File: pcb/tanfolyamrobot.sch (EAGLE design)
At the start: 86 parts, among them IC1 STM32F10XRXT6, IC2 7805, IC4 FT232RL, IC5 LD117AS33TR, M1 DRV8833, Q1 AO4407A, Q2 BSS123, Q3 BSS123, Q4 BSS123, X1 CSTCE08M, X2 PWR, X6 KUSBVX-BS1N

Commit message: fixed silkscreen
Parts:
- renumbered JP1 to SWD, JP16 to SERVO, LED1 to TX, LED2 to RX, S1 to RST, S2 to BUT, VR1 to CONT

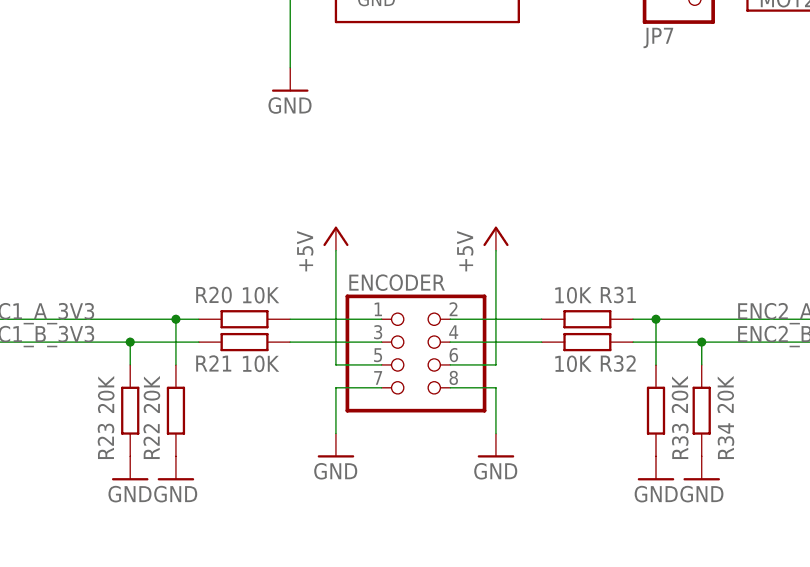
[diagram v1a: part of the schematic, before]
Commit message: fixed encoder connector silkscreen
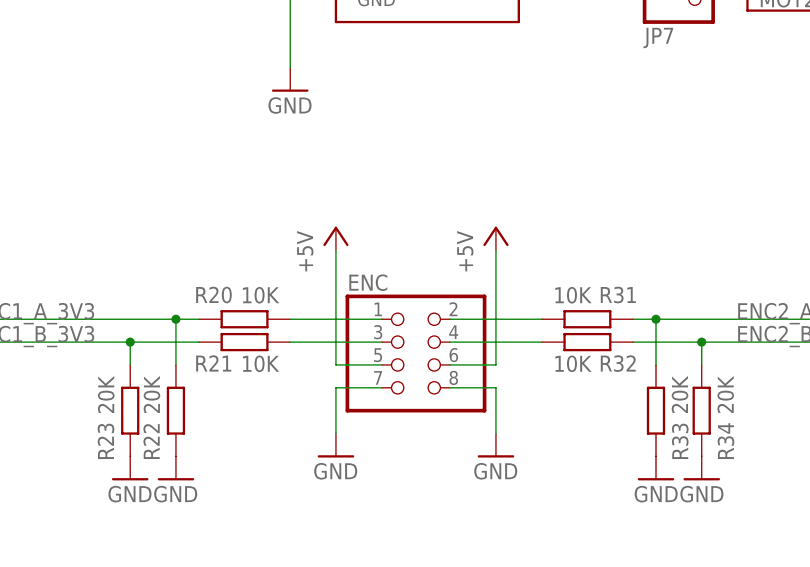
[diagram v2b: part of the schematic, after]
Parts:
- renumbered ENCODER to ENC
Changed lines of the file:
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@@
 <part name="IC5" library="v-reg" library_urn="urn:adsk.eagle:library:409" deviceset="LD117A?*" device="S" package3d_urn="urn:adsk.eagle:package:30370/1" technology="33TR"/>
 <part name="SERVO" library="pinhead" library_urn="urn:adsk.eagle:library:325" deviceset="PINHD-1X3" device="/90" package3d_urn="urn:adsk.eagle:package:22459/2"/>
-<part name="ENCODER" library="pinhead" library_urn="urn:adsk.eagle:library:325" deviceset="PINHD-2X4" device="/90" package3d_urn="urn:adsk.eagle:package:22465/2"/>
+<part name="ENC" library="pinhead" library_urn="urn:adsk.eagle:library:325" deviceset="PINHD-2X4" device="/90" package3d_urn="urn:adsk.eagle:package:22465/2"/>
 <part name="P+12" library="supply1" library_urn="urn:adsk.eagle:library:371" deviceset="+5V" device=""/>
 <part name="GND29" library="supply1" library_urn="urn:adsk.eagle:library:371" deviceset="GND" device=""/>
@@
 <attribute name="VALUE" x="468.63" y="45.72" size="1.778" layer="96"/>
 </instance>
-<instance part="ENCODER" gate="A" x="347.98" y="83.82" smashed="yes">
+<instance part="ENC" gate="A" x="347.98" y="83.82" smashed="yes">
 <attribute name="NAME" x="341.63" y="92.075" size="1.778" layer="95"/>
 <attribute name="VALUE" x="341.63" y="76.2" size="1.778" layer="96"/>
@@
 <wire x1="340.36" y1="81.28" x2="340.36" y2="76.2" width="0.1524" layer="91"/>
 <pinref part="GND16" gate="1" pin="GND"/>
-<pinref part="ENCODER" gate="A" pin="7"/>
+<pinref part="ENC" gate="A" pin="7"/>
 </segment>
 <segment>
@@
 </segment>
 <segment>
-<pinref part="ENCODER" gate="A" pin="8"/>
+<pinref part="ENC" gate="A" pin="8"/>
 <wire x1="353.06" y1="81.28" x2="358.14" y2="81.28" width="0.1524" layer="91"/>
 <pinref part="GND29" gate="1" pin="GND"/>
@@
 <wire x1="345.44" y1="83.82" x2="340.36" y2="83.82" width="0.1524" layer="91"/>
 <pinref part="P+6" gate="1" pin="+5V"/>
-<pinref part="ENCODER" gate="A" pin="5"/>
+<pinref part="ENC" gate="A" pin="5"/>
 </segment>
 <segment>
@@
 </segment>
 <segment>
-<pinref part="ENCODER" gate="A" pin="6"/>
+<pinref part="ENC" gate="A" pin="6"/>
 <wire x1="353.06" y1="83.82" x2="358.14" y2="83.82" width="0.1524" layer="91"/>
 <pinref part="P+12" gate="1" pin="+5V"/>
@@
 <wire x1="345.44" y1="88.9" x2="335.28" y2="88.9" width="0.1524" layer="91"/>
 <pinref part="R20" gate="G$1" pin="1"/>
-<pinref part="ENCODER" gate="A" pin="1"/>
+<pinref part="ENC" gate="A" pin="1"/>
 </segment>
 </net>
@@
 <wire x1="345.44" y1="86.36" x2="335.28" y2="86.36" width="0.1524" layer="91"/>
 <pinref part="R21" gate="G$1" pin="1"/>
-<pinref part="ENCODER" gate="A" pin="3"/>
+<pinref part="ENC" gate="A" pin="3"/>
 </segment>
 </net>
@@
 <wire x1="353.06" y1="86.36" x2="363.22" y2="86.36" width="0.1524" layer="91"/>
 <pinref part="R32" gate="G$1" pin="1"/>
-<pinref part="ENCODER" gate="A" pin="4"/>
+<pinref part="ENC" gate="A" pin="4"/>
 </segment>
 </net>
@@
 <wire x1="353.06" y1="88.9" x2="363.22" y2="88.9" width="0.1524" layer="91"/>
 <pinref part="R31" gate="G$1" pin="1"/>
-<pinref part="ENCODER" gate="A" pin="2"/>
-</segment>
-</net>
+<pinref part="ENC" gate="A" pin="2"/>
+</segment>
+</net>

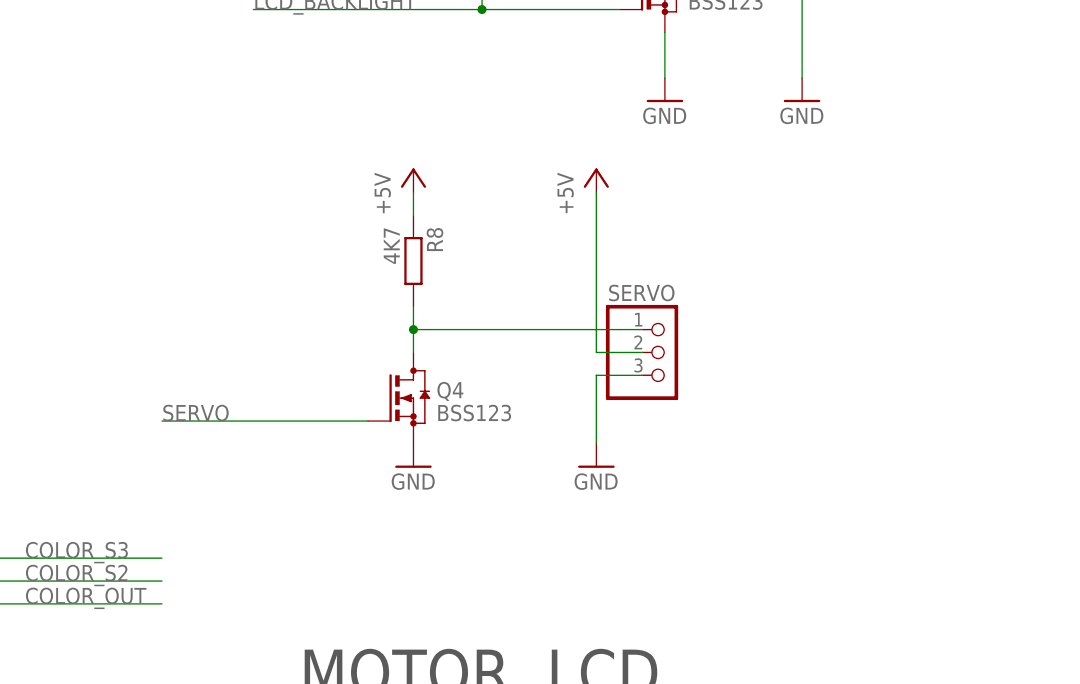
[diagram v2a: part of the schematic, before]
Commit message: changed servo signal pin pullup value (#1)
The signal pin can draw some current, so a low resistance pullup is
needed
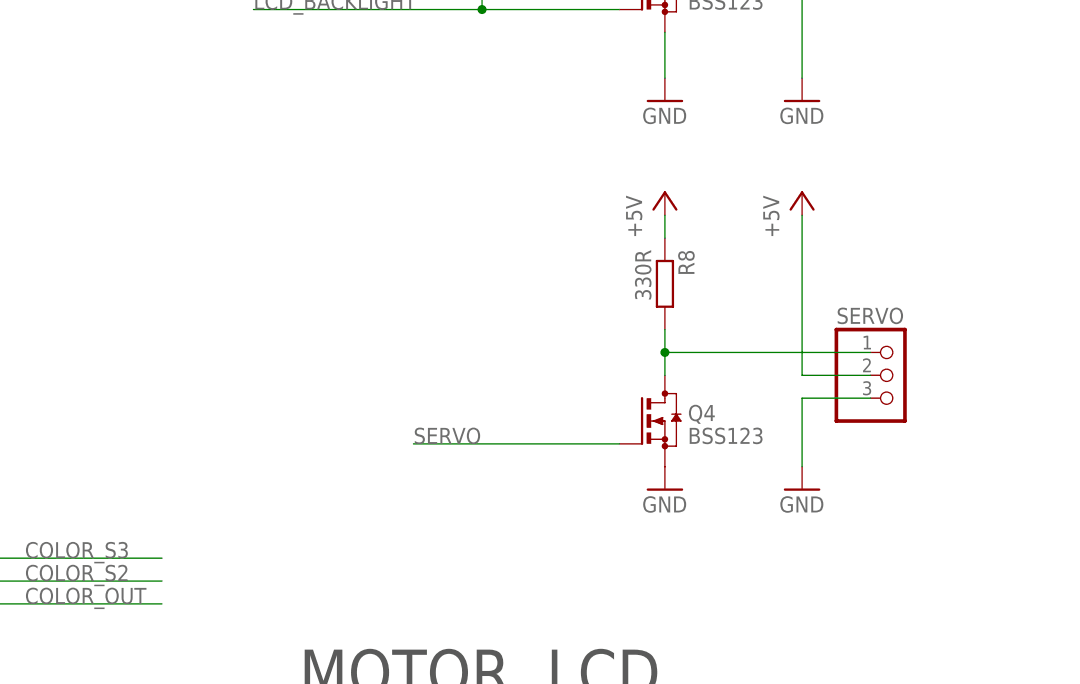
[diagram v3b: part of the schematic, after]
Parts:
- R8: value 4K7 -> 330R
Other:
- note added: "The signal pin can draw some current, so a low resistance pullup is needed"
- moved on the sheet: Q4, R8, SERVO
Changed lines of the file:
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@@
 <part name="GND30" library="supply1" library_urn="urn:adsk.eagle:library:371" deviceset="GND" device=""/>
 <part name="Q4" library="transistor-small-signal" library_urn="urn:adsk.eagle:library:401" deviceset="BSS123" device="" package3d_urn="urn:adsk.eagle:package:28738/2"/>
-<part name="R8" library="rcl" library_urn="urn:adsk.eagle:library:334" deviceset="R-EU_" device="R0603" package3d_urn="urn:adsk.eagle:package:23555/3" value="4K7"/>
+<part name="R8" library="rcl" library_urn="urn:adsk.eagle:library:334" deviceset="R-EU_" device="R0603" package3d_urn="urn:adsk.eagle:package:23555/3" value="330R"/>
 <part name="P+13" library="supply1" library_urn="urn:adsk.eagle:library:371" deviceset="+5V" device=""/>
 <part name="P+14" library="supply1" library_urn="urn:adsk.eagle:library:371" deviceset="+5V" device=""/>
@@
 <text x="480.06" y="228.6" size="1.778" layer="97">The ESP8266's reset signal
 is actually active-low.</text>
+<text x="426.72" y="58.42" size="1.778" layer="150">The signal pin can draw some current,
+so a low resistance pullup is needed</text>
 </plain>
 <instances>
@@
 <attribute name="VALUE" x="170.18" y="48.26" size="1.778" layer="96"/>
 </instance>
-<instance part="SERVO" gate="A" x="474.98" y="53.34" smashed="yes">
-<attribute name="NAME" x="468.63" y="59.055" size="1.778" layer="95"/>
-<attribute name="VALUE" x="468.63" y="45.72" size="1.778" layer="96"/>
+<instance part="SERVO" gate="A" x="500.38" y="50.8" smashed="yes">
+<attribute name="NAME" x="494.03" y="56.515" size="1.778" layer="95"/>
+<attribute name="VALUE" x="494.03" y="43.18" size="1.778" layer="96"/>
 </instance>
 <instance part="ENC" gate="A" x="347.98" y="83.82" smashed="yes">
@@
 <attribute name="VALUE" x="355.6" y="71.12" size="1.778" layer="96"/>
 </instance>
-<instance part="GND30" gate="1" x="467.36" y="40.64" smashed="yes">
-<attribute name="VALUE" x="464.82" y="38.1" size="1.778" layer="96"/>
-</instance>
-<instance part="Q4" gate="G$1" x="447.04" y="48.26" smashed="yes">
-<attribute name="NAME" x="449.58" y="48.26" size="1.778" layer="95"/>
-<attribute name="VALUE" x="449.58" y="45.72" size="1.778" layer="96"/>
-</instance>
-<instance part="R8" gate="G$1" x="447.04" y="63.5" smashed="yes" rot="R270">
-<attribute name="NAME" x="448.5386" y="67.31" size="1.778" layer="95" rot="R270"/>
-<attribute name="VALUE" x="443.738" y="67.31" size="1.778" layer="96" rot="R270"/>
-</instance>
-<instance part="P+13" gate="1" x="447.04" y="73.66" smashed="yes">
-<attribute name="VALUE" x="444.5" y="68.58" size="1.778" layer="96" rot="R90"/>
-</instance>
-<instance part="P+14" gate="1" x="467.36" y="73.66" smashed="yes">
-<attribute name="VALUE" x="464.82" y="68.58" size="1.778" layer="96" rot="R90"/>
-</instance>
-<instance part="GND31" gate="1" x="447.04" y="40.64" smashed="yes">
-<attribute name="VALUE" x="444.5" y="38.1" size="1.778" layer="96"/>
+<instance part="GND30" gate="1" x="490.22" y="38.1" smashed="yes">
+<attribute name="VALUE" x="487.68" y="35.56" size="1.778" layer="96"/>
+</instance>
+<instance part="Q4" gate="G$1" x="474.98" y="45.72" smashed="yes">
+<attribute name="NAME" x="477.52" y="45.72" size="1.778" layer="95"/>
+<attribute name="VALUE" x="477.52" y="43.18" size="1.778" layer="96"/>
+</instance>
+<instance part="R8" gate="G$1" x="474.98" y="60.96" smashed="yes" rot="R270">
+<attribute name="NAME" x="476.4786" y="64.77" size="1.778" layer="95" rot="R270"/>
+<attribute name="VALUE" x="471.678" y="64.77" size="1.778" layer="96" rot="R270"/>
+</instance>
+<instance part="P+13" gate="1" x="474.98" y="71.12" smashed="yes">
+<attribute name="VALUE" x="472.44" y="66.04" size="1.778" layer="96" rot="R90"/>
+</instance>
+<instance part="P+14" gate="1" x="490.22" y="71.12" smashed="yes">
+<attribute name="VALUE" x="487.68" y="66.04" size="1.778" layer="96" rot="R90"/>
+</instance>
+<instance part="GND31" gate="1" x="474.98" y="38.1" smashed="yes">
+<attribute name="VALUE" x="472.44" y="35.56" size="1.778" layer="96"/>
 </instance>
 <instance part="GND32" gate="1" x="474.98" y="81.28" smashed="yes">
@@
 <segment>
 <pinref part="SERVO" gate="A" pin="3"/>
-<wire x1="472.44" y1="50.8" x2="467.36" y2="50.8" width="0.1524" layer="91"/>
+<wire x1="497.84" y1="48.26" x2="490.22" y2="48.26" width="0.1524" layer="91"/>
 <pinref part="GND30" gate="1" pin="GND"/>
-<wire x1="467.36" y1="50.8" x2="467.36" y2="43.18" width="0.1524" layer="91"/>
+<wire x1="490.22" y1="48.26" x2="490.22" y2="40.64" width="0.1524" layer="91"/>
 </segment>
 <segment>
@@
 <segment>
 <pinref part="SERVO" gate="A" pin="2"/>
-<wire x1="472.44" y1="53.34" x2="467.36" y2="53.34" width="0.1524" layer="91"/>
+<wire x1="497.84" y1="50.8" x2="490.22" y2="50.8" width="0.1524" layer="91"/>
 <pinref part="P+14" gate="1" pin="+5V"/>
-<wire x1="467.36" y1="53.34" x2="467.36" y2="71.12" width="0.1524" layer="91"/>
+<wire x1="490.22" y1="50.8" x2="490.22" y2="68.58" width="0.1524" layer="91"/>
 </segment>
 <segment>
 <pinref part="R8" gate="G$1" pin="1"/>
 <pinref part="P+13" gate="1" pin="+5V"/>
-<wire x1="447.04" y1="71.12" x2="447.04" y2="68.58" width="0.1524" layer="91"/>
+<wire x1="474.98" y1="68.58" x2="474.98" y2="66.04" width="0.1524" layer="91"/>
 </segment>
 <segment>
@@
 <pinref part="R8" gate="G$1" pin="2"/>
 <pinref part="Q4" gate="G$1" pin="D"/>
-<wire x1="447.04" y1="58.42" x2="447.04" y2="55.88" width="0.1524" layer="91"/>
+<wire x1="474.98" y1="55.88" x2="474.98" y2="53.34" width="0.1524" layer="91"/>
 <pinref part="SERVO" gate="A" pin="1"/>
-<wire x1="447.04" y1="55.88" x2="447.04" y2="53.34" width="0.1524" layer="91"/>
-<wire x1="472.44" y1="55.88" x2="447.04" y2="55.88" width="0.1524" layer="91"/>
-<junction x="447.04" y="55.88"/>
+<wire x1="474.98" y1="53.34" x2="474.98" y2="50.8" width="0.1524" layer="91"/>
+<wire x1="497.84" y1="53.34" x2="474.98" y2="53.34" width="0.1524" layer="91"/>
+<junction x="474.98" y="53.34"/>
 </segment>
 </net>
@@
 <segment>
 <pinref part="Q4" gate="G$1" pin="G"/>
-<wire x1="441.96" y1="45.72" x2="419.1" y2="45.72" width="0.1524" layer="91"/>
-<label x="419.1" y="45.72" size="1.778" layer="95"/>
-</segment>
-<segment>
+<wire x1="469.9" y1="43.18" x2="447.04" y2="43.18" width="0.1524" layer="91"/>
+<label x="447.04" y="43.18" size="1.778" layer="95"/>
+</segment>
+<segment>
